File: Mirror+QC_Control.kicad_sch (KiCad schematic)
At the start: 29 parts, among them J1 3220-10-0300-00, J2 Screw_Terminal_01x04, J3 Screw_Terminal_01x06, U1 LT1012, U10 LT1012, U11 LT1012, U2 LM4040DBZ-2.0, U3 LT1012, U4 LM4040DBZ-2.0, U5 LT1012, U6 LT1012, U7 Teensy4.0

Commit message: changes after DR1
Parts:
- added C10, C11, C12, C13, C14, C15, C4, C5, C6, C7, C8, C9: 0.1muF, Capacitor_SMD:C_0805_2012Metric, symbol Device:C
- added C16, C17, C18: C, Capacitor_SMD:C_0805_2012Metric, symbol Device:C
- added D1, D2, D3: 5962-XL-2012UGCTR-ND, LED_SMD:LED_0805_2012Metric, symbol Device:LED
- added H1, H2, H3, H4: MountingHole_Pad_MP, MountingHole:MountingHole_3.2mm_M3_DIN965_Pad_TopBottom, symbol Mechanical:MountingHole_Pad_MP
- added R13, R14: 1300, Resistor_SMD:R_0805_2012Metric, symbol Device:R
- added R17: 300, Resistor_SMD:R_0805_2012Metric, symbol Device:R
- added TP1, TP2, TP3, TP4, TP5, TP6, TP7, TP8, TP9: TestPoint, TestPoint:TestPoint_Pad_2.0x2.0mm, symbol Connector:TestPoint
- J1: value 3220-10-0300-00 -> FSM
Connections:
- net +15V: now also C10.2, C12.2, C13.2, C4.1, C7.2, C8.2, D1.2 (A)
- net +5V: now also D3.2 (A); no longer U7.33 (VIN)
- net -15V: now also C11.2, C14.2, C15.2, C5.1, C6.2, C9.2, D2.2 (A)
- net GND: now also U7.1 (GND), U7.17 (GND), U7.47 (GND), C10.1, C11.1, C12.1, C13.1, C14.1, C15.1, C4.2, C5.2, C6.1, C7.1, C8.1, C9.1, H1.MP, H2.MP, H3.MP, H4.MP, R13.1, R14.2, R17.2, TP7.1, TP8.1, TP9.1
- net sum_stage1: now reaches C3.2, R15.1, R4.2, U5.6
- net sum_stage1: now also TP2.1
- net at R15.2, R16.1, U6.2 (-): now also C18.1
- net y_stage1: now reaches C2.2, R10.1, R9.2, U1.6
- net y_stage1: now also TP5.1
- net at R10.2, R11.1, U3.2 (-): now also C17.1
- net x_stage1: now reaches C1.2, R2.2, R5.1, U10.6
- net x_stage1: now also TP6.1
- net at R5.2, R6.1, U11.2 (-): now also C16.1
- net y_stage2: now reaches R11.2, U3.6, U7.22 (15_A1_RX3_SPDIF_IN)
- net y_stage2: now also C17.2, TP4.1
- net sum_stage2: now reaches R16.2, U6.6, U7.23 (16_A2_RX4_SCL1)
- net sum_stage2: now also C18.2, TP1.1
- net x_stage2: now reaches R6.2, U11.6, U7.21 (14_A0_TX3_SPDIF_OUT)
- net x_stage2: now also C16.2, TP3.1
- new net: D1.1 (K), R13.2
- new net: D3.1 (K), R17.1
- new net: D2.1 (K), R14.1
- no-connect marks 0 -> 61
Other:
- title: (none) -> Teensy Control of QC and FSM
- moved on the sheet: C1, C2, C3, R1, R10, R11, R12, R15, R16, R2, R3, R4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

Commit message: changes since DR2
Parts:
- removed U4: LM4040DBZ-2.0, Package_TO_SOT_SMD:SOT-23, symbol Reference_Voltage:LM4040DBZ-2.0
- added GND4: TP_GND4, TestPoint:TestPoint_Loop_D3.50mm_Drill1.4mm_Beaded, symbol Connector:TestPoint
- added R18, R20: 750, Capacitor_SMD:C_0805_2012Metric, symbol Device:R
- added R19, R21: 10k, Capacitor_SMD:C_0805_2012Metric, symbol Device:R
- added TP_DIN1: TP_DIN, TestPoint:TestPoint_Loop_D3.50mm_Drill1.4mm_Beaded, symbol Connector:TestPoint
- added TP_EN1: TP_EN, TestPoint:TestPoint_Loop_D3.50mm_Drill1.4mm_Beaded, symbol Connector:TestPoint
- added TP_SYNC1: TP_SYNC, TestPoint:TestPoint_Loop_D3.50mm_Drill1.4mm_Beaded, symbol Connector:TestPoint
- added U8: LM4040DBZ-2.0, Package_TO_SOT_SMD:SOT-23, symbol Reference_Voltage:LM4040DBZ-2.0
- C10, C11, C12, C13, C14, C15, C4, C5, C6, C7, C8, C9: value 0.1muF -> 0.1uF
- GND1: renamed from TP9; value TestPoint -> TP_GND1; footprint TestPoint:TestPoint_Pad_2.0x2.0mm -> TestPoint:TestPoint_Loop_D3.50mm_Drill1.4mm_Beaded
- GND2: renamed from TP8; value TestPoint -> TP_GND2; footprint TestPoint:TestPoint_Pad_2.0x2.0mm -> TestPoint:TestPoint_Loop_D3.50mm_Drill1.4mm_Beaded
- GND3: renamed from TP7; value TestPoint -> TP_GND3; footprint TestPoint:TestPoint_Pad_2.0x2.0mm -> TestPoint:TestPoint_Loop_D3.50mm_Drill1.4mm_Beaded
- J1: value FSM -> FSM Driver
- SumStage1: renamed from TP2; value TestPoint -> TP_sumstage1; footprint TestPoint:TestPoint_Pad_2.0x2.0mm -> TestPoint:TestPoint_Loop_D3.50mm_Drill1.4mm_Beaded
- SumStage2: renamed from TP1; value TestPoint -> TP_sumstage2; footprint TestPoint:TestPoint_Pad_2.0x2.0mm -> TestPoint:TestPoint_Loop_D3.50mm_Drill1.4mm_Beaded
- XStage1: renamed from TP6; value TestPoint -> TP_xstage1; footprint TestPoint:TestPoint_Pad_2.0x2.0mm -> TestPoint:TestPoint_Loop_D3.50mm_Drill1.4mm_Beaded
- XStage2: renamed from TP3; value TestPoint -> TP_xstage2; footprint TestPoint:TestPoint_Pad_2.0x2.0mm -> TestPoint:TestPoint_Loop_D3.50mm_Drill1.4mm_Beaded
- YStage1: renamed from TP5; value TestPoint -> TP_ystage1; footprint TestPoint:TestPoint_Pad_2.0x2.0mm -> TestPoint:TestPoint_Loop_D3.50mm_Drill1.4mm_Beaded
- YStage2: renamed from TP4; value TestPoint -> TP_ystage2; footprint TestPoint:TestPoint_Pad_2.0x2.0mm -> TestPoint:TestPoint_Loop_D3.50mm_Drill1.4mm_Beaded
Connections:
- net +5V: now also R18.1, R20.1; no longer U2.2 (A)
- net -15V: now also D2.1 (K); no longer D2.2 (A)
- net DIN: now also TP_DIN1.1
- net EN: now also TP_EN1.1
- net GND: now also U2.2 (A), GND4.1, R19.2, R21.2, U8.2 (A)
- net SYNC: now also TP_SYNC1.1
- net at R3.1, U2.1 (K): now also R18.2, R19.1
- net at R8.1: now also R20.2, R21.1, U8.1 (K)
- net at R14.1: now also D2.2 (A); no longer D2.1 (K)
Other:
- moved on the sheet: D2, U2

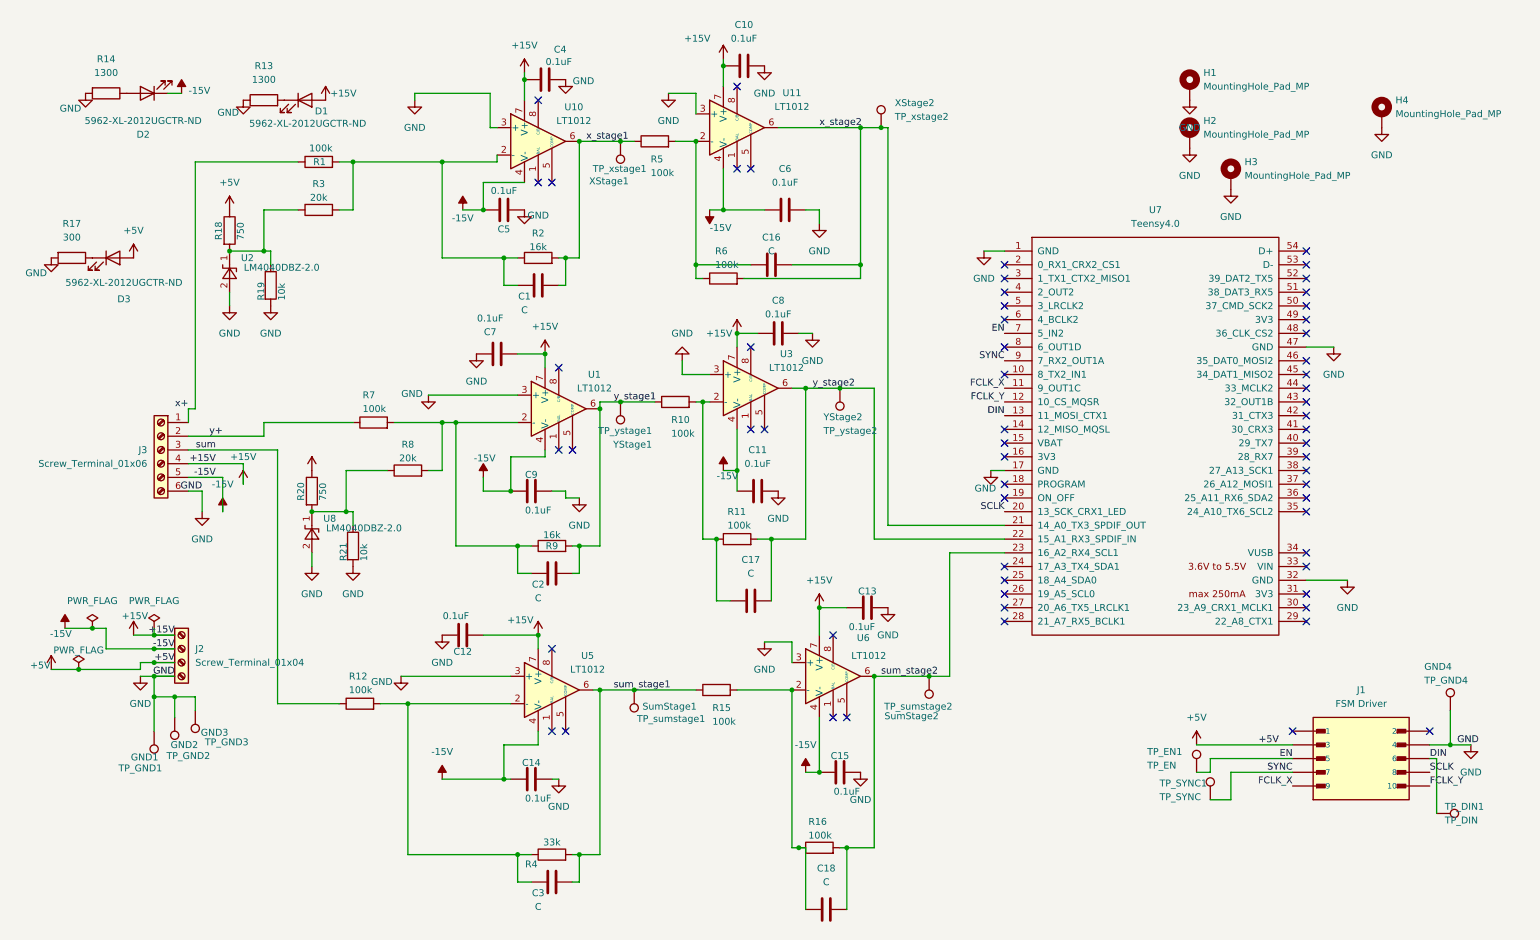
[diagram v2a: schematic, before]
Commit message: added LCSC values and refined silkscreen. still missing capacitor values for LPFs
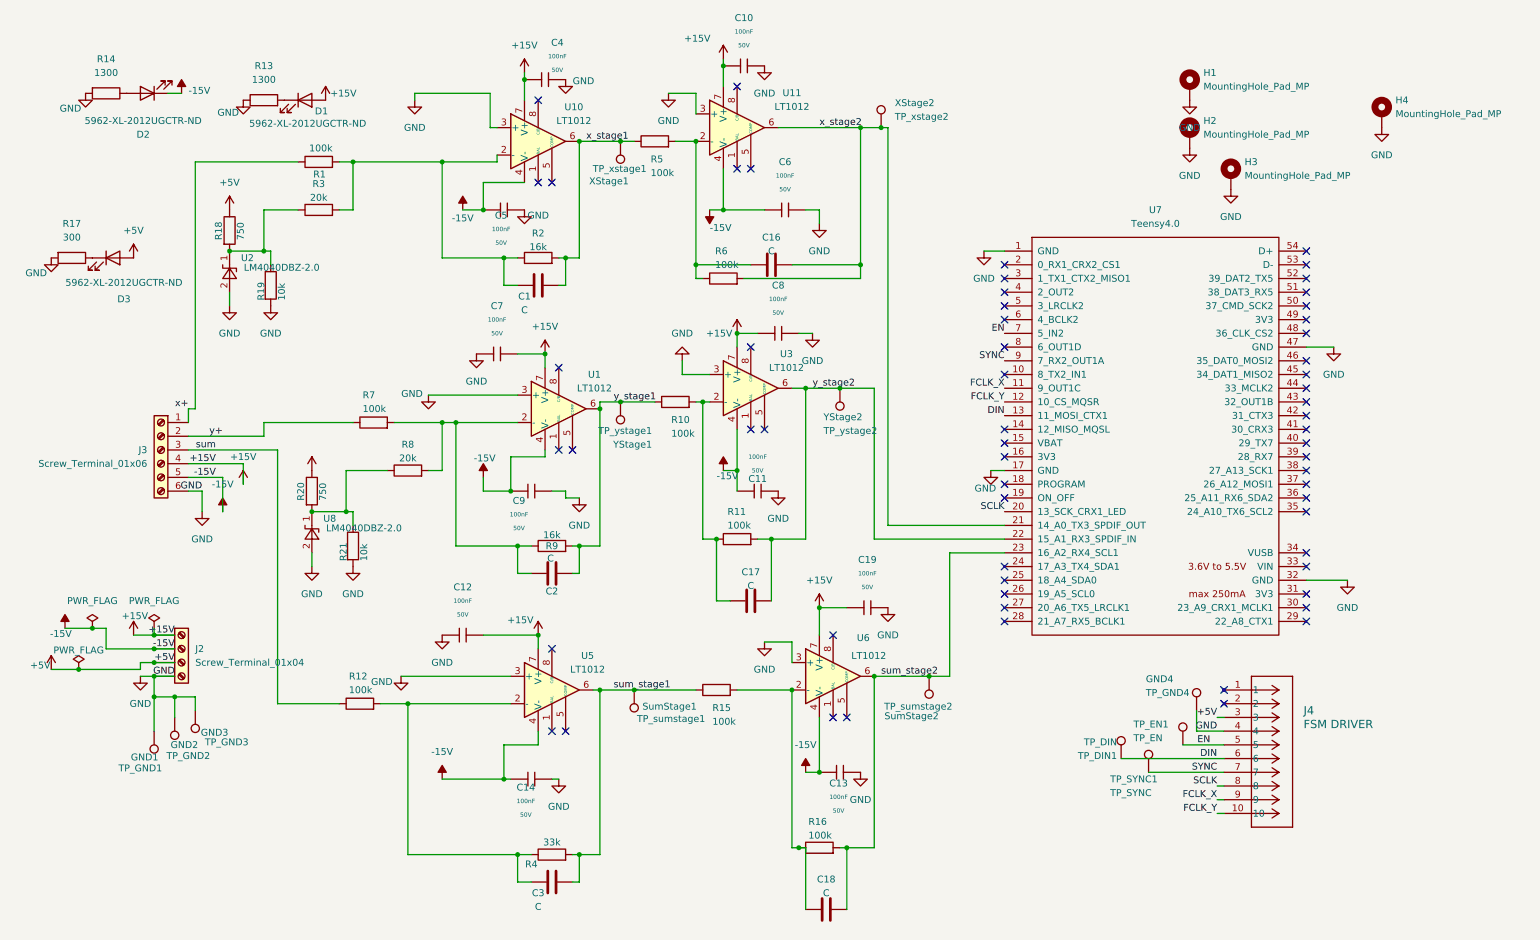
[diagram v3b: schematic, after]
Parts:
- removed C10, C11, C12, C13, C14, C15, C4, C5, C6, C7, C8, C9: 0.1uF, Capacitor_SMD:C_0805_2012Metric, symbol Device:C
- removed J1: FSM Driver, 3220-10-0300-00:CNC_3220-10-0300-00, symbol 3220-10-0300-00:3220-10-0300-00
- added C10, C11, C12, C13, C14, C19, C4, C5, C6, C7, C8, C9: 100nF, PCM_JLCPCB:C_0603, symbol JLCPCB-Capacitors:0603,100nF
- added J4: FSM DRIVER, CONN_3220-10-0100-00_CNC, symbol FSM:3220-10-0100-00
- C2: footprint Capacitor_SMD:C_0805_2012Metric -> (none)
- R1, R10, R11, R12, R15, R16, R5, R6, R7: footprint Resistor_SMD:R_0805_2012Metric -> Resistor_SMD:R_0603_1608Metric; LCSC (none) -> C14675
- R18, R20: footprint Capacitor_SMD:C_0805_2012Metric -> Capacitor_SMD:C_0603_1608Metric; LCSC (none) -> C2907066
- R19, R21: footprint Capacitor_SMD:C_0805_2012Metric -> Capacitor_SMD:C_0603_1608Metric; LCSC (none) -> C2930027
- R2, R9: footprint Resistor_SMD:R_0805_2012Metric -> Resistor_SMD:R_0603_1608Metric; LCSC (none) -> C2907107
- R3, R8: footprint Resistor_SMD:R_0805_2012Metric -> Resistor_SMD:R_0603_1608Metric; LCSC (none) -> C2907011
- R4: footprint Resistor_SMD:R_0805_2012Metric -> Resistor_SMD:R_0603_1608Metric; LCSC (none) -> C2907028
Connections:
- net +15V: now also C10.1, C12.2, C19.1, C4.1, C7.2, C8.1
- net +5V: now also J4.3
- net -15V: now also C11.1, C13.1, C14.1, C5.1, C6.1, C9.1
- net DIN: now also J4.6
- net EN: now also J4.5
- net FCLK_X: now also J4.9
- net FCLK_Y: now also J4.10
- net GND: now also C10.2, C11.2, C12.1, C13.2, C14.2, C19.2, C4.2, C5.2, C6.2, C7.1, C8.2, C9.2, J4.4
- net SCLK: now also J4.8
- net SYNC: now also J4.7
- net y_stage1: now also C2.1; no longer C2.2
- net at R7.2, R8.2, R9.1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: now also C2.2; no longer C2.1
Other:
- moved on the sheet: GND4, TP_DIN1, TP_EN1, TP_SYNC1

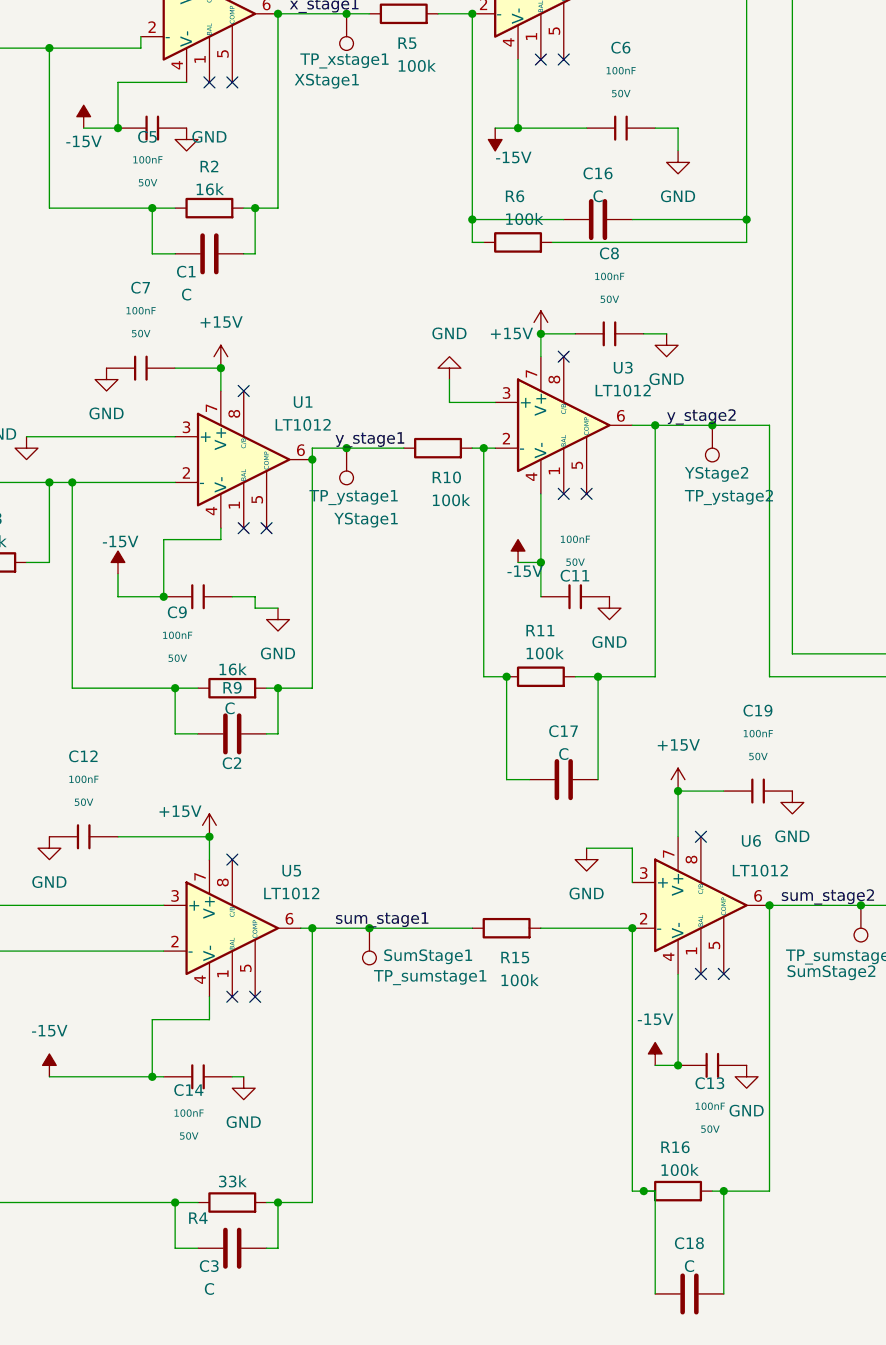
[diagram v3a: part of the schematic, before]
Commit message: changes include capacitance values for LPFs
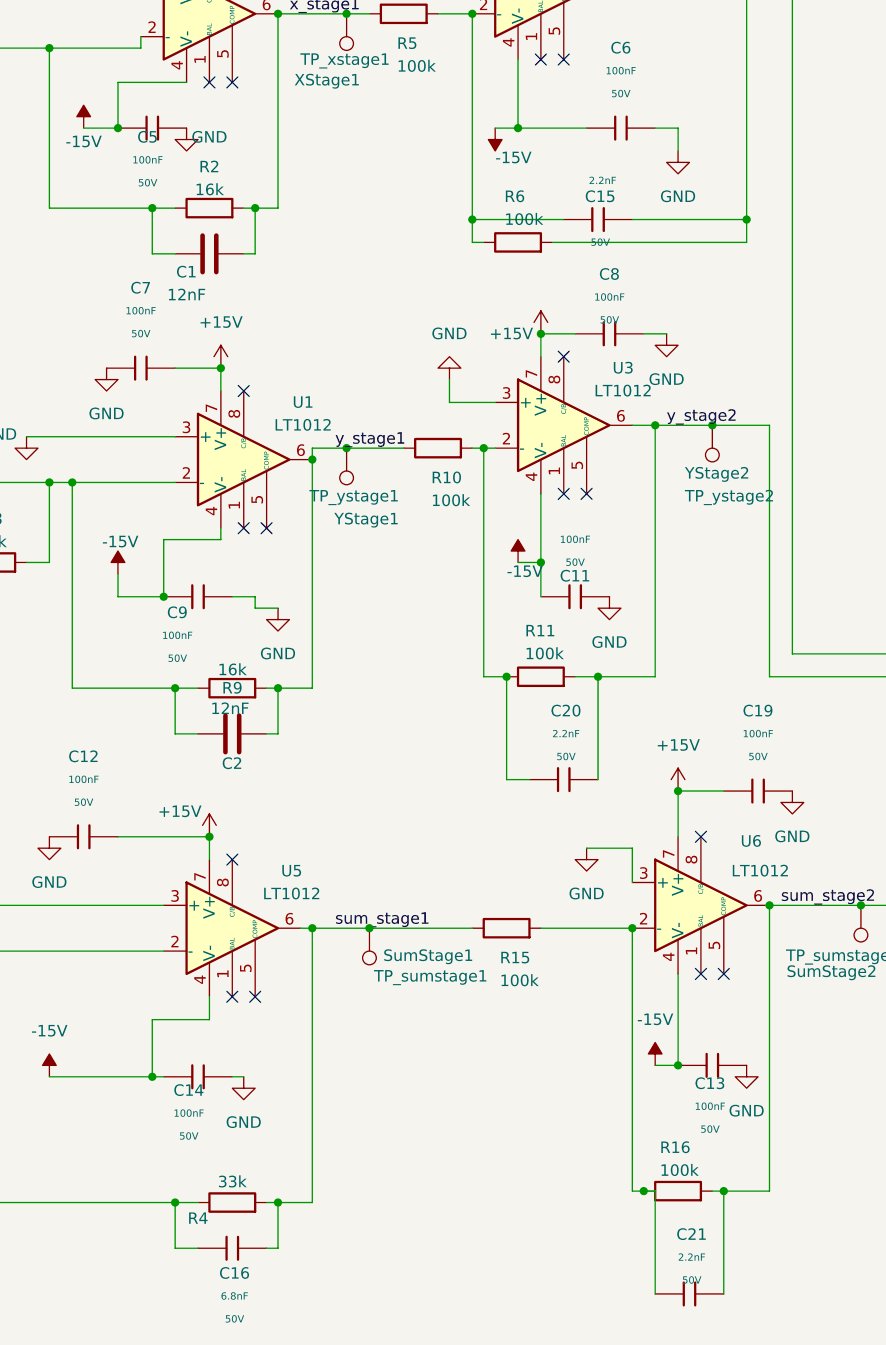
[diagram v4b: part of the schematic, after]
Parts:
- removed C16, C17, C18, C3: C, Capacitor_SMD:C_0805_2012Metric, symbol Device:C
- added C15, C20, C21: 2.2nF, PCM_JLCPCB:C_0603, symbol JLCPCB-Capacitors:0603,2.2nF
- added C16: 6.8nF, PCM_JLCPCB:C_0603, symbol JLCPCB-Capacitors:0603,6.8nF
- C1: value C -> 12nF; footprint Capacitor_SMD:C_0805_2012Metric -> Capacitor_SMD:C_0603_1608Metric; LCSC (none) -> C107074
- C2: value C -> 12nF; footprint (none) -> Capacitor_SMD:C_0603_1608Metric; LCSC (none) -> C107074
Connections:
- net sum_stage1: now also C16.2
- net sum_stage2: now also C21.2
- net x_stage2: now also C15.2
- net y_stage2: now also C20.2
- net at R15.2, R16.1, U6.2 (-): now also C21.1
- net at R10.2, R11.1, U3.2 (-): now also C20.1
- net at R5.2, R6.1, U11.2 (-): now also C15.1
- net at R12.2, R4.1, U5.2 (-): now also C16.1

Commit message: final changes to board with nice layout
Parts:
- U1, U10, U11, U3, U5, U6: footprint Package_SO:SOIC-8_3.9x4.9mm_P1.27mm -> Package_DIP:DIP-8_W7.62mm; LCSC (none) -> C305904
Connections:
- net +15V: now also J2.2 (Pin_2), J3.2 (Pin_2); no longer J2.1 (Pin_1), J3.4 (Pin_4)
- net +5V: now also J2.4 (Pin_4); no longer J2.3 (Pin_3)
- net -15V: now also J2.3 (Pin_3), J3.3 (Pin_3); no longer J2.2 (Pin_2), J3.5 (Pin_5)
- net GND: now also J2.1 (Pin_1), J3.1 (Pin_1); no longer J2.4 (Pin_4), J3.6 (Pin_6)
- net sum: now also J3.6 (Pin_6); no longer J3.3 (Pin_3)
- net x+: now also J3.4 (Pin_4); no longer J3.1 (Pin_1)
- net y+: now also J3.5 (Pin_5); no longer J3.2 (Pin_2)
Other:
- moved on the sheet: GND1, GND2, GND3, J2

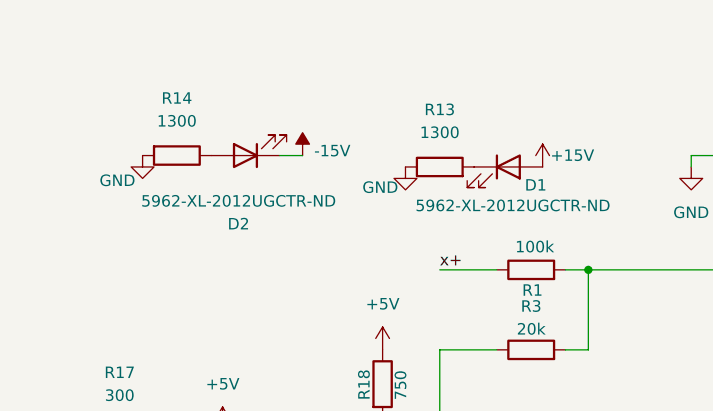
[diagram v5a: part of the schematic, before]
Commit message: adding all LCSC part numbers
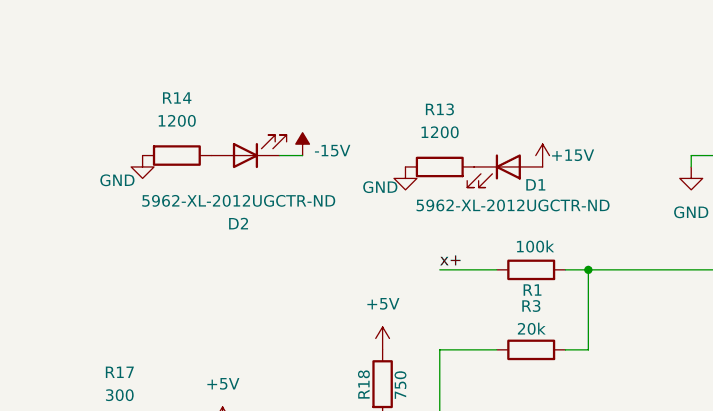
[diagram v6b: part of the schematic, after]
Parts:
- D1, D2, D3: LCSC (none) -> C965815
- GND1, GND2, GND3, GND4, SumStage1, SumStage2, TP_DIN1, TP_EN1, TP_SYNC1, XStage1, XStage2, YStage1, YStage2: footprint TestPoint:TestPoint_Loop_D3.50mm_Drill1.4mm_Beaded -> TestPoint:TestPoint_Loop_D2.60mm_Drill1.6mm_Beaded; LCSC (none) -> C2906763
- J2: LCSC (none) -> C5443561
- J3: LCSC (none) -> C2915642
- J4: LCSC (none) -> C7501289
- R13, R14: value 1300 -> 1200; LCSC (none) -> C114526
- R17: LCSC (none) -> C17617
- U2, U8: LCSC (none) -> C431732
- U7: now left out of the parts list
